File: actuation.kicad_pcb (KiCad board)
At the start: 4 copper layers, 130 x 130 mm, 320 parts, among them J1 ACTUATION, J10 ACT CH9, J11 ACT CH10, J12 ACT CH11, J13 ACT CH12, J14 ACT CH13, J15 ACT CH14, J16 ACT CH15, J17 ACT CH16, J18 FB CH1, J19 FB CH2, J2 ACT CH1, J20 FB CH3, J21 VDET CH1, J22 VDET CH2, J23 PWR IN, J24 PWR PROT, J25 PWR 3.3V, J26 SAFETY, J27 ARM, J28 ACT HOT, J29 ACT COLD, J3 ACT CH2, J4 ACT CH3, J5 ACT CH4, J6 ACT CH5, J7 ACT CH6, J8 ACT CH7, J9 ACT CH8, K1 J115F11C, Q1 SI7220 NMOS, Q2 NMOS, U1 TPD4E02B04DQA, U10 TLP241A, U11 TLP241A, U12 TLP241A, U13 TLP241A, U14 TLP241A, U15 TLP241A, U16 TLP241A, U17 TLP241A, U18 TLP241A, U19 PCA9534, U2 PCA9615, U20 PCA9534, U21 TLP2366, U22 TLP2366, U23 TLP2366, U24 TLP2366, U25 TLP2366, U26 TLP2366, U27 TLV7031, U28 TLV7031, U29 TLP2366, U3 TLP241A, U30 TLP2366, U31 74LVC1G126, U32 74LVC1G126, U33 PCA9534, U34 SN74LVC541A, U35 TLI4971, U36 LTC4367, U37 ADS1110, U38 AP64350, U39 TLP241A, U4 TLP241A, U40 LP5912-3.3DRV, U5 TLP241A, U6 TLP241A, U7 TLP241A, U8 TLP241A, U9 TLP241A

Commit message: cameron adjustments, 3.3 plane
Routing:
- net GND: track 116.4 -> 105.8 mm
- net /Power/COIL+: track 65.3 -> 66.9 mm
- added copper zone on In2.Cu, net +3.3V
- removed copper zone on In2.Cu, net GND

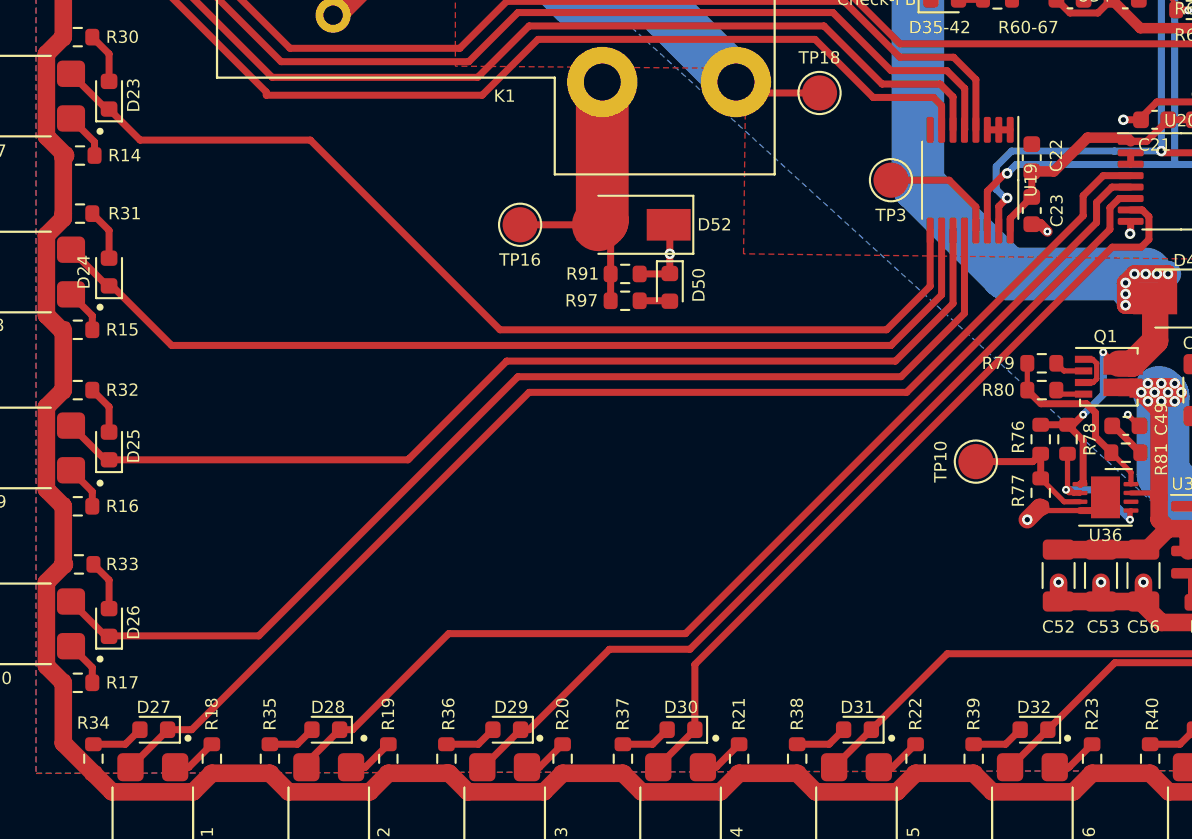
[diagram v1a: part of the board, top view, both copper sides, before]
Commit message: moved some traces
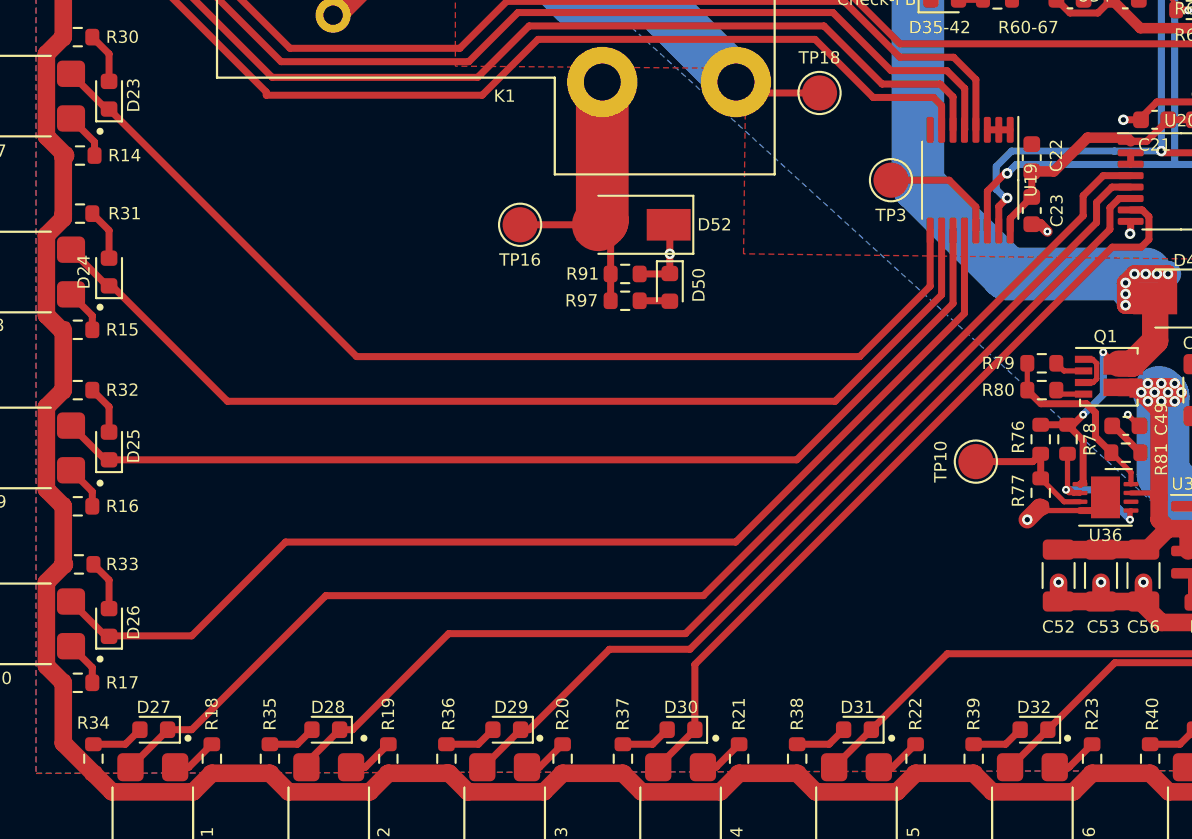
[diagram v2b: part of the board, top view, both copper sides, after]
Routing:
- net /Actuator Channels/ACT_CH6: track 56.6 -> 59.2 mm
- net /Actuator Channels/ACT_CH5: track 59.1 -> 60.3 mm
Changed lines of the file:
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@@
   (segment (start 104.013 89.2555) (end 104.013 87.567) (width 0.4) (layer "F.Cu") (net 36))
   (segment (start 104.013 100.7365) (end 103.8565 100.7365) (width 0.4) (layer "F.Cu") (net 37))
+  (segment (start 118.0845 114.808) (end 146.685 114.808) (width 0.4) (layer "F.Cu") (net 37))
   (segment (start 150.689 110.804) (end 150.689 107.6425) (width 0.4) (layer "F.Cu") (net 37))
-  (segment (start 115.454 102.5) (end 105.7765 102.5) (width 0.4) (layer "F.Cu") (net 37))
-  (segment (start 148.209 113.284) (end 150.689 110.804) (width 0.4) (layer "F.Cu") (net 37))
   (segment (start 103.8565 100.7365) (end 101.85 98.73) (width 0.4) (layer "F.Cu") (net 37))
-  (segment (start 115.454 102.5) (end 126.238 113.284) (width 0.4) (layer "F.Cu") (net 37))
-  (segment (start 126.238 113.284) (end 148.209 113.284) (width 0.4) (layer "F.Cu") (net 37))
-  (segment (start 105.7765 102.5) (end 104.013 100.7365) (width 0.4) (layer "F.Cu") (net 37))
+  (segment (start 146.685 114.808) (end 150.689 110.804) (width 0.4) (layer "F.Cu") (net 37))
+  (segment (start 104.013 100.7365) (end 118.0845 114.808) (width 0.4) (layer "F.Cu") (net 37))
   (segment (start 104.013 97.6) (end 103.06 96.647) (width 0.4) (layer "F.Cu") (net 38))
   (segment (start 104.013 99.1615) (end 104.013 97.6) (width 0.4) (layer "F.Cu") (net 38))
+  (segment (start 104.1835 110.7875) (end 104.013 110.7875) (width 0.4) (layer "F.Cu") (net 39))
+  (segment (start 145.288 117.348) (end 110.744 117.348) (width 0.4) (layer "F.Cu") (net 39))
+  (segment (start 151.339 111.297) (end 145.288 117.348) (width 0.4) (layer "F.Cu") (net 39))
+  (segment (start 103.9075 110.7875) (end 101.85 108.73) (width 0.4) (layer "F.Cu") (net 39))
   (segment (start 151.339 107.6425) (end 151.339 111.297) (width 0.4) (layer "F.Cu") (net 39))
-  (segment (start 151.339 111.297) (end 148.463 114.173) (width 0.4) (layer "F.Cu") (net 39))
-  (segment (start 103.9075 110.7875) (end 101.85 108.73) (width 0.4) (layer "F.Cu") (net 39))
   (segment (start 104.013 110.7875) (end 103.9075 110.7875) (width 0.4) (layer "F.Cu") (net 39))
-  (segment (start 107.569 114.173) (end 104.1835 110.7875) (width 0.4) (layer "F.Cu") (net 39))
-  (segment (start 148.463 114.173) (end 107.569 114.173) (width 0.4) (layer "F.Cu") (net 39))
-  (segment (start 104.1835 110.7875) (end 104.013 110.7875) (width 0.4) (layer "F.Cu") (net 39))
+  (segment (start 110.744 117.348) (end 104.1835 110.7875) (width 0.4) (layer "F.Cu") (net 39))
   (segment (start 104.013 109.2125) (end 104.013 107.633) (width 0.4) (layer "F.Cu") (net 40))
   (segment (start 104.013 107.633) (end 103.06 106.68) (width 0.4) (layer "F.Cu") (net 40))
   (segment (start 151.989 111.79) (end 151.989 107.6425) (width 0.4) (layer "F.Cu") (net 41))
   (segment (start 104.013 120.6755) (end 103.7955 120.6755) (width 0.4) (layer "F.Cu") (net 41))
-  (segment (start 148.717 115.062) (end 151.989 111.79) (width 0.4) (layer "F.Cu") (net 41))
-  (segment (start 121.0055 120.6755) (end 121.0945 120.5865) (width 0.4) (layer "F.Cu") (net 41))
-  (segment (start 126.619 115.062) (end 148.717 115.062) (width 0.4) (layer "F.Cu") (net 41))
-  (segment (start 104.013 120.6755) (end 121.0055 120.6755) (width 0.4) (layer "F.Cu") (net 41))
+  (segment (start 104.013 120.6755) (end 143.1035 120.6755) (width 0.4) (layer "F.Cu") (net 41))
+  (segment (start 143.1035 120.6755) (end 151.989 111.79) (width 0.4) (layer "F.Cu") (net 41))
   (segment (start 103.7955 120.6755) (end 101.85 118.73) (width 0.4) (layer "F.Cu") (net 41))
-  (segment (start 121.0945 120.5865) (end 126.619 115.062) (width 0.4) (layer "F.Cu") (net 41))
   (segment (start 104.013 117.666) (end 103.06 116.713) (width 0.4) (layer "F.Cu") (net 42))
   (segment (start 104.013 119.1005) (end 104.013 117.666) (width 0.4) (layer "F.Cu") (net 42))
   (segment (start 103.8285 130.7085) (end 101.85 128.73) (width 0.4) (layer "F.Cu") (net 43))
-  (segment (start 112.522 130.683) (end 104.0385 130.683) (width 0.4) (layer "F.Cu") (net 43))
+  (segment (start 108.712 130.683) (end 104.0385 130.683) (width 0.4) (layer "F.Cu") (net 43))
+  (segment (start 114.046 125.349) (end 108.712 130.683) (width 0.4) (layer "F.Cu") (net 43))
+  (segment (start 152.639 112.3465) (end 139.6365 125.349) (width 0.4) (layer "F.Cu") (net 43))
+  (segment (start 104.013 130.7085) (end 103.8285 130.7085) (width 0.4) (layer "F.Cu") (net 43))
+  (segment (start 139.6365 125.349) (end 114.046 125.349) (width 0.4) (layer "F.Cu") (net 43))
+  (segment (start 152.639 107.6425) (end 152.639 112.3465) (width 0.4) (layer "F.Cu") (net 43))
   (segment (start 104.0385 130.683) (end 104.013 130.7085) (width 0.4) (layer "F.Cu") (net 43))
-  (segment (start 127.254 115.951) (end 112.522 130.683) (width 0.4) (layer "F.Cu") (net 43))
-  (segment (start 104.013 130.7085) (end 103.8285 130.7085) (width 0.4) (layer "F.Cu") (net 43))
-  (segment (start 152.639 112.3465) (end 149.0345 115.951) (width 0.4) (layer "F.Cu") (net 43))
-  (segment (start 152.639 107.6425) (end 152.639 112.3465) (width 0.4) (layer "F.Cu") (net 43))
-  (segment (start 149.0345 115.951) (end 127.254 115.951) (width 0.4) (layer "F.Cu") (net 43))
   (segment (start 104.013 127.508) (end 103.124 126.619) (width 0.4) (layer "F.Cu") (net 44))
   (segment (start 104.013 129.1335) (end 104.013 127.508) (width 0.4) (layer "F.Cu") (net 44))
+  (segment (start 137.795 128.397) (end 159.385 106.807) (width 0.4) (layer "F.Cu") (net 45))
   (segment (start 159.385 106.807) (end 159.385 105.664) (width 0.4) (layer "F.Cu") (net 45))
+  (segment (start 107.3405 136.0395) (end 105.23 138.15) (width 0.4) (layer "F.Cu") (net 45))
   (segment (start 107.3405 136.017) (end 108.712 136.017) (width 0.4) (layer "F.Cu") (net 45))
+  (segment (start 107.3405 136.017) (end 107.3405 136.0395) (width 0.4) (layer "F.Cu") (net 45))
+  (segment (start 108.712 136.017) (end 116.332 128.397) (width 0.4) (layer "F.Cu") (net 45))
   (segment (start 159.385 105.664) (end 160.528 104.521) (width 0.4) (layer "F.Cu") (net 45))
-  (segment (start 108.712 136.017) (end 127.889 116.84) (width 0.4) (layer "F.Cu") (net 45))
-  (segment (start 107.3405 136.0395) (end 105.23 138.15) (width 0.4) (layer "F.Cu") (net 45))
+  (segment (start 116.332 128.397) (end 137.795 128.397) (width 0.4) (layer "F.Cu") (net 45))
   (segment (start 160.528 104.521) (end 162.0865 104.521) (width 0.4) (layer "F.Cu") (net 45))
-  (segment (start 149.352 116.84) (end 159.385 106.807) (width 0.4) (layer "F.Cu") (net 45))
-  (segment (start 107.3405 136.017) (end 107.3405 136.0395) (width 0.4) (layer "F.Cu") (net 45))
-  (segment (start 127.889 116.84) (end 149.352 116.84) (width 0.4) (layer "F.Cu") (net 45))
   (segment (start 104.9395 136.843) (end 105.7655 136.017) (width 0.4) (layer "F.Cu") (net 46))
   (segment (start 103.124 136.843) (end 104.9395 136.843) (width 0.4) (layer "F.Cu") (net 46))
@@
     (connect_pads yes (clearance 0.2))
     (min_thickness 0.2) (filled_areas_thickness no)
-    (fill (thermal_gap 0.508) (thermal_bridge_width 0.508))
+    (fill yes (thermal_gap 0.508) (thermal_bridge_width 0.508))
     (polygon
       (pts
@@
     (connect_pads yes (clearance 0.2))
     (min_thickness 0.2) (filled_areas_thickness no)
-    (fill (thermal_gap 0.508) (thermal_bridge_width 0.508))
+    (fill yes (thermal_gap 0.508) (thermal_bridge_width 0.508))
     (polygon
       (pts
@@
     (connect_pads yes (clearance 0.2))
     (min_thickness 0.2) (filled_areas_thickness no)
-    (fill (thermal_gap 0.508) (thermal_bridge_width 0.508))
+    (fill yes (thermal_gap 0.508) (thermal_bridge_width 0.508))
     (polygon
       (pts
@@
     (connect_pads yes (clearance 0.2))
     (min_thickness 0.2) (filled_areas_thickness no)
-    (fill (thermal_gap 0.508) (thermal_bridge_width 0.508))
+    (fill yes (thermal_gap 0.508) (thermal_bridge_width 0.508))
     (polygon
       (pts
@@
     (connect_pads yes (clearance 0.2))
     (min_thickness 0.2) (filled_areas_thickness no)
-    (fill (thermal_gap 0.508) (thermal_bridge_width 0.508))
+    (fill yes (thermal_gap 0.508) (thermal_bridge_width 0.508))
     (polygon
       (pts
@@
     (connect_pads yes (clearance 0.508))
     (min_thickness 0.254) (filled_areas_thickness no)
-    (fill (thermal_gap 0.508) (thermal_bridge_width 0.508))
+    (fill yes (thermal_gap 0.508) (thermal_bridge_width 0.508))
     (polygon
       (pts
@@
     (connect_pads yes (clearance 0.2))
     (min_thickness 0.2) (filled_areas_thickness no)
-    (fill (thermal_gap 0.508) (thermal_bridge_width 0.508))
+    (fill yes (thermal_gap 0.508) (thermal_bridge_width 0.508))
     (polygon
       (pts
@@
     (connect_pads yes (clearance 0.2))
     (min_thickness 0.2) (filled_areas_thickness no)
-    (fill (thermal_gap 0.508) (thermal_bridge_width 0.508))
+    (fill yes (thermal_gap 0.508) (thermal_bridge_width 0.508))
     (polygon
       (pts
@@
     (connect_pads yes (clearance 0.2))
     (min_thickness 0.2) (filled_areas_thickness no)
-    (fill (thermal_gap 0.508) (thermal_bridge_width 0.508))
+    (fill yes (thermal_gap 0.508) (thermal_bridge_width 0.508))
     (polygon
       (pts

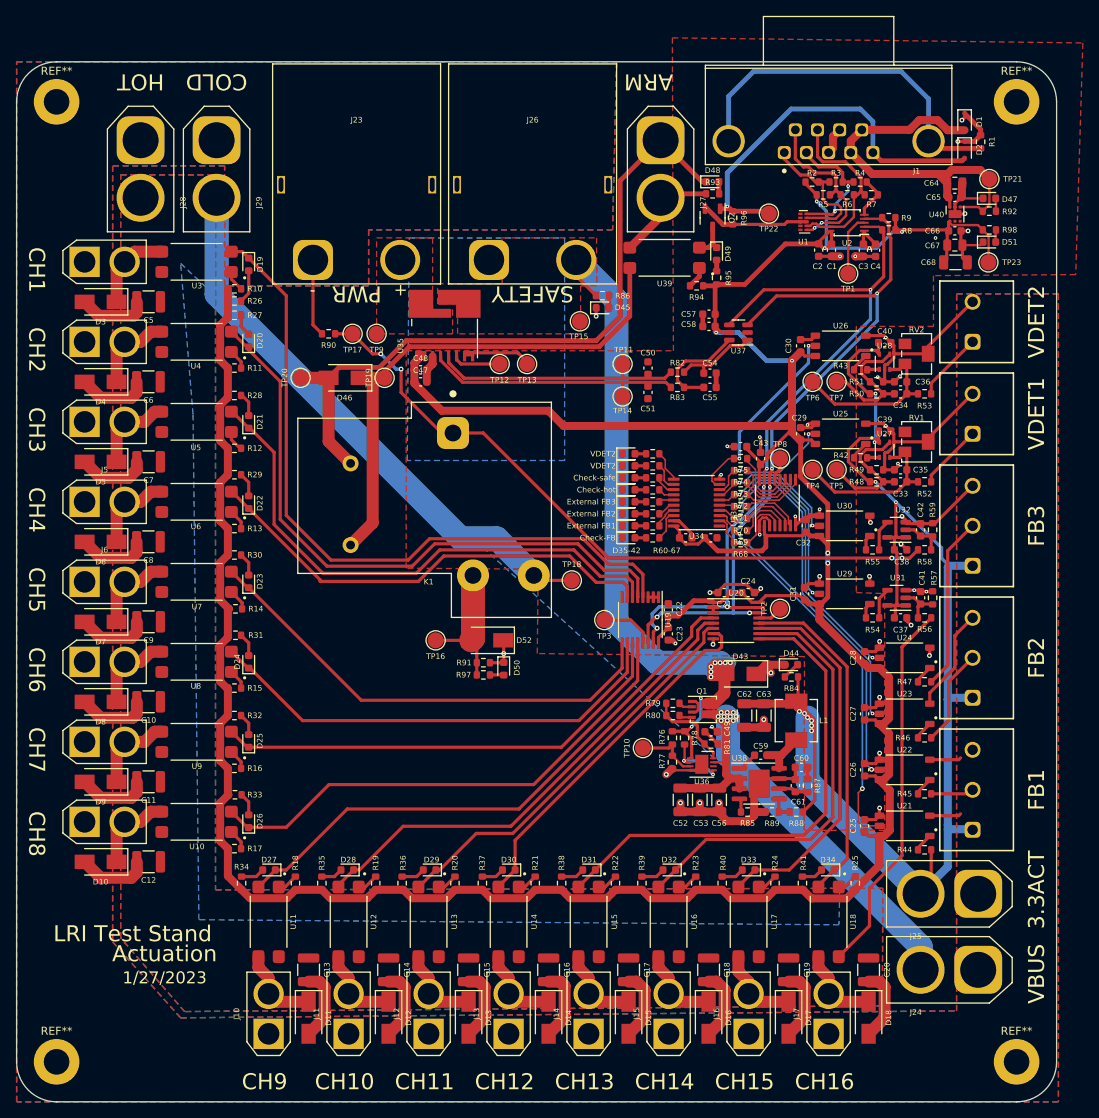
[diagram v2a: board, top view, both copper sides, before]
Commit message: fix silkscreens, planes
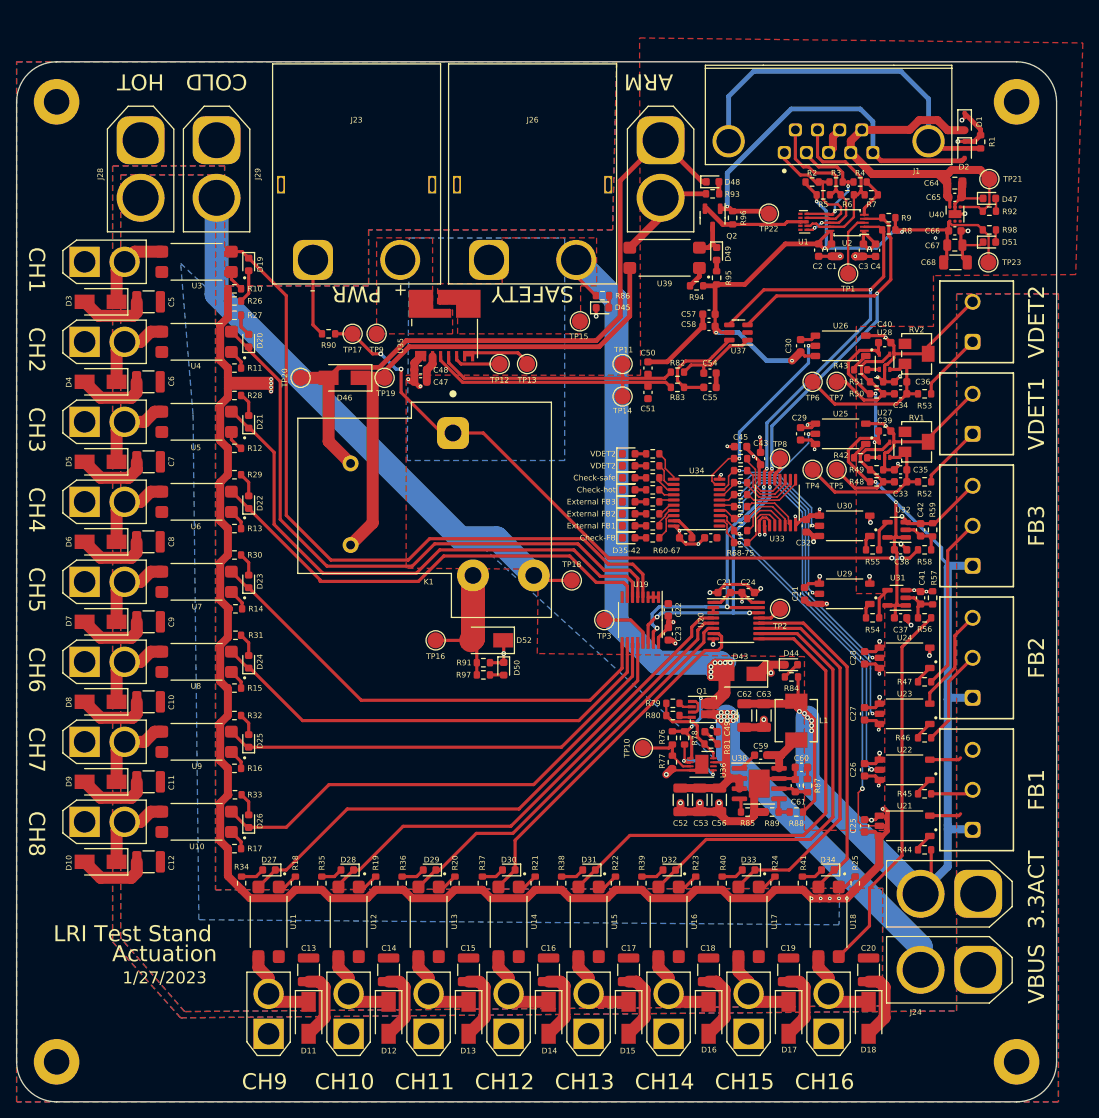
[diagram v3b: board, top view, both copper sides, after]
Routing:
- net +3.3V: track 460.4 -> 339.0 mm, vias 8 -> 30
- net GND: track 105.8 -> 113.5 mm
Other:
- board text added: "R68-75"

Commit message: stitching vias
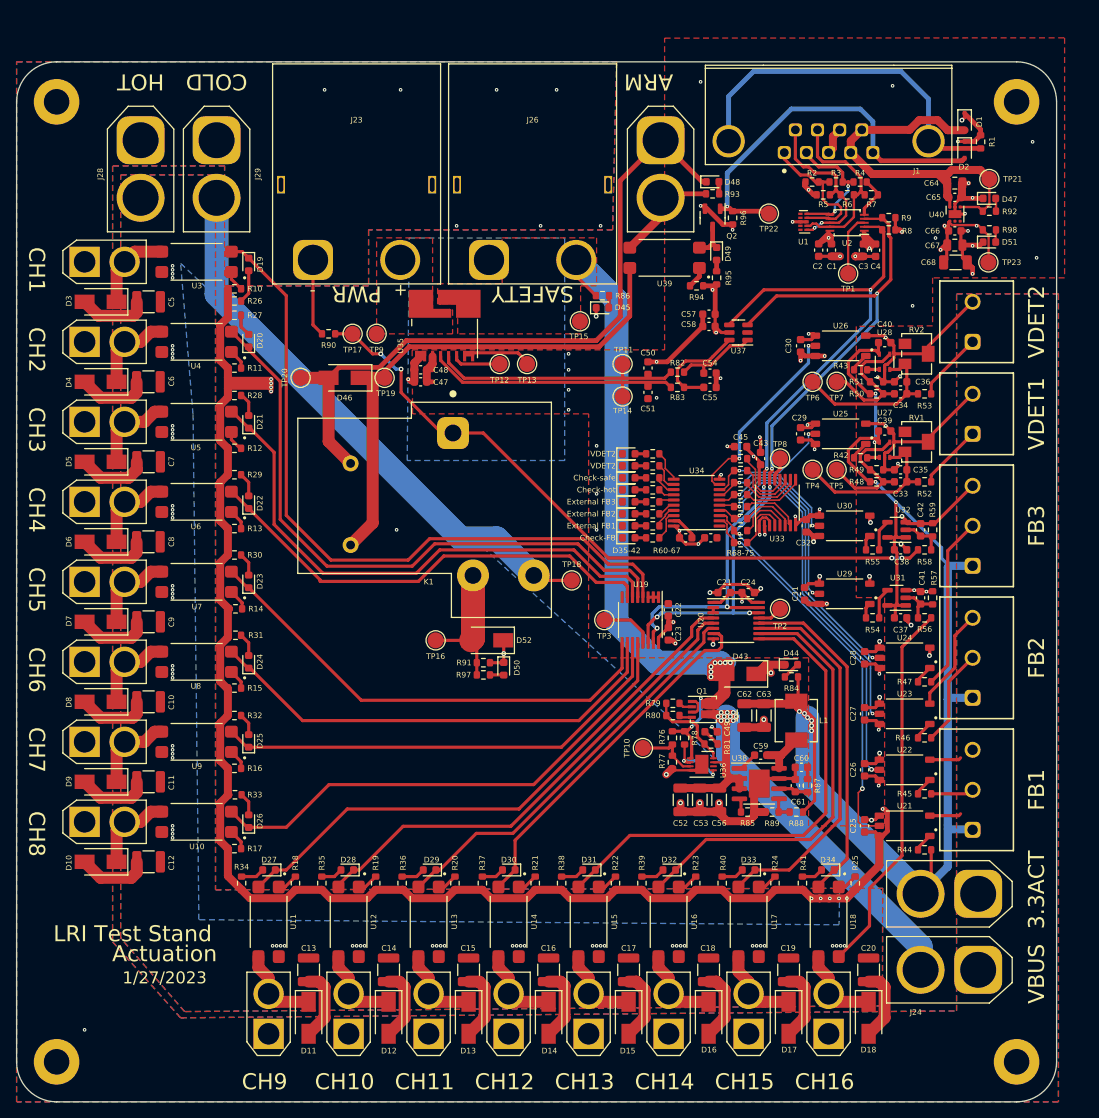
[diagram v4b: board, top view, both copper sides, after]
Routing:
- net +3.3V: track 339.0 -> 294.0 mm, vias 30 -> 34
- net GND: track 113.5 -> 112.6 mm, vias 23 -> 46
- net Vdrive: vias 0 -> 64
- net GNDPWR: vias 22 -> 31
